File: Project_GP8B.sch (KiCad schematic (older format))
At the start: 11 parts, among them U1 74AHC05, U2 74AHC05, U3 74AHC1G04, U4 74AHC1G04, U5 74AHC05

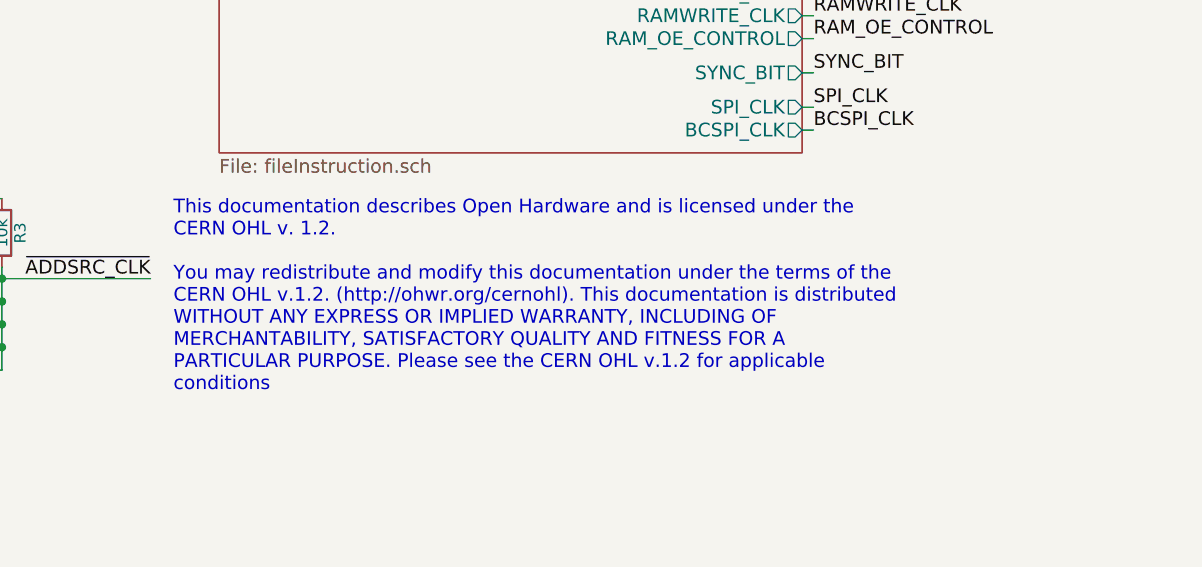
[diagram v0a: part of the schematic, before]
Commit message: Switching license to "CERN-OHLw v2 or later"
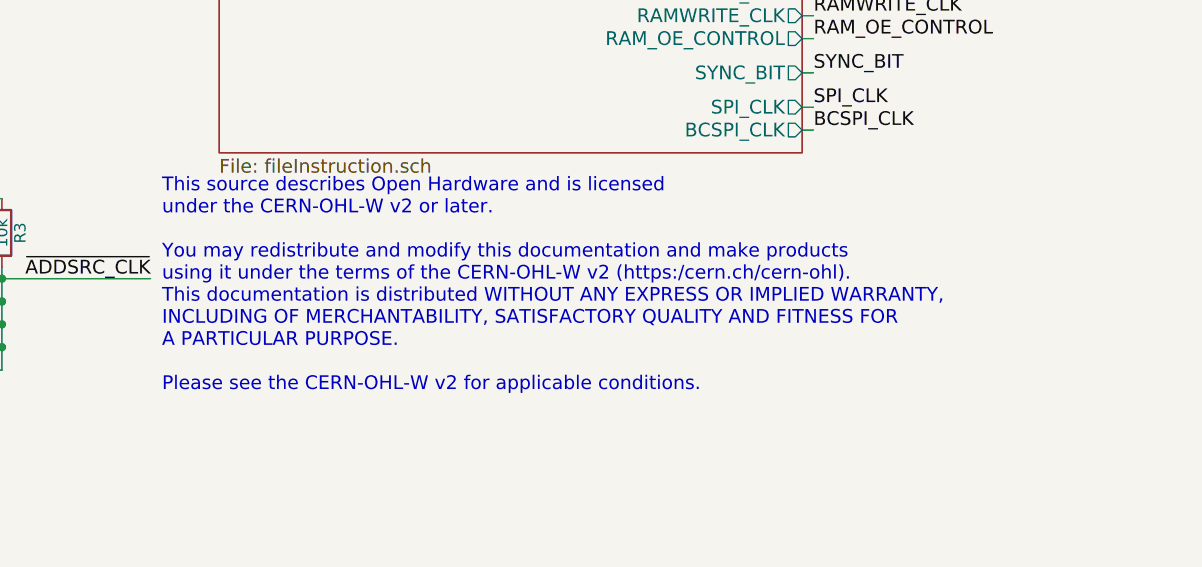
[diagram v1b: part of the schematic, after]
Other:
- note added: "This source describes Open Hardware and is licensed\nunder the CERN-OHL-W v2 or later. \n\nYou may redistribute and modify this documentation and make products\nusing it under the terms of the CERN-OHL-W v2 (https:/cern.ch/cern-ohl).\nThis documentation is distributed WITHOUT ANY EXPRESS OR IMPLIED WARRANTY,\nINCLUDING OF MERCHANTABILITY, SATISFACTORY QUALITY AND FITNESS FOR\nA PARTICULAR PURPOSE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"
- note removed: "This documentation describes Open Hardware and is licensed under the\nCERN OHL v. 1.2.\n\nYou may redistribute and modify this documentation under the terms of the\nCERN OHL v.1.2. (http://ohwr.org/cernohl). This documentation is distributed\nWITHOUT ANY EXPRESS OR IMPLIED WARRANTY, INCLUDING OF\nMERCHANTABILITY, SATISFACTORY QUALITY AND FITNESS FOR A\nPARTICULAR PURPOSE. Please see the CERN OHL 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"
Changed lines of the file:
@@
 Comp "Guillaume Guillet"
 Comment1 "Copyright Guillaume Guillet 2020"
-Comment2 "Licensed under CERN OHL v.1.2"
+Comment2 "Licensed under CERN-OHL-W v2 or later"
 Comment3 ""
 Comment4 ""
@@
 Text Label 10350 5300 0    60   ~ 0
 BCSPI_CLK
-Text Notes 7550 6450 0    60   ~ 0
-This documentation describes Open Hardware and is licensed under the\nCERN OHL v. 1.2.\n\nYou may redistribute and modify this documentation under the terms of the\nCERN OHL v.1.2. (http://ohwr.org/cernohl). This documentation is distributed\nWITHOUT ANY EXPRESS OR IMPLIED WARRANTY, INCLUDING OF\nMERCHANTABILITY, SATISFACTORY QUALITY AND FITNESS FOR A\nPARTICULAR PURPOSE. Please see the CERN OHL v.1.2 for applicable\nconditions
+Text Notes 7500 6450 0    60   ~ 0
+This source describes Open Hardware and is licensed\nunder the CERN-OHL-W v2 or later. \n\nYou may redistribute and modify this documentation and make products\nusing it under the terms of the CERN-OHL-W v2 (https:/cern.ch/cern-ohl).\nThis documentation is distributed WITHOUT ANY EXPRESS OR IMPLIED WARRANTY,\nINCLUDING OF MERCHANTABILITY, SATISFACTORY QUALITY AND FITNESS FOR\nA PARTICULAR PURPOSE.\n\nPlease see the CERN-OHL-W v2 for applicable conditions.
 Wire Bus Line
 	1700 2800 1700 3600

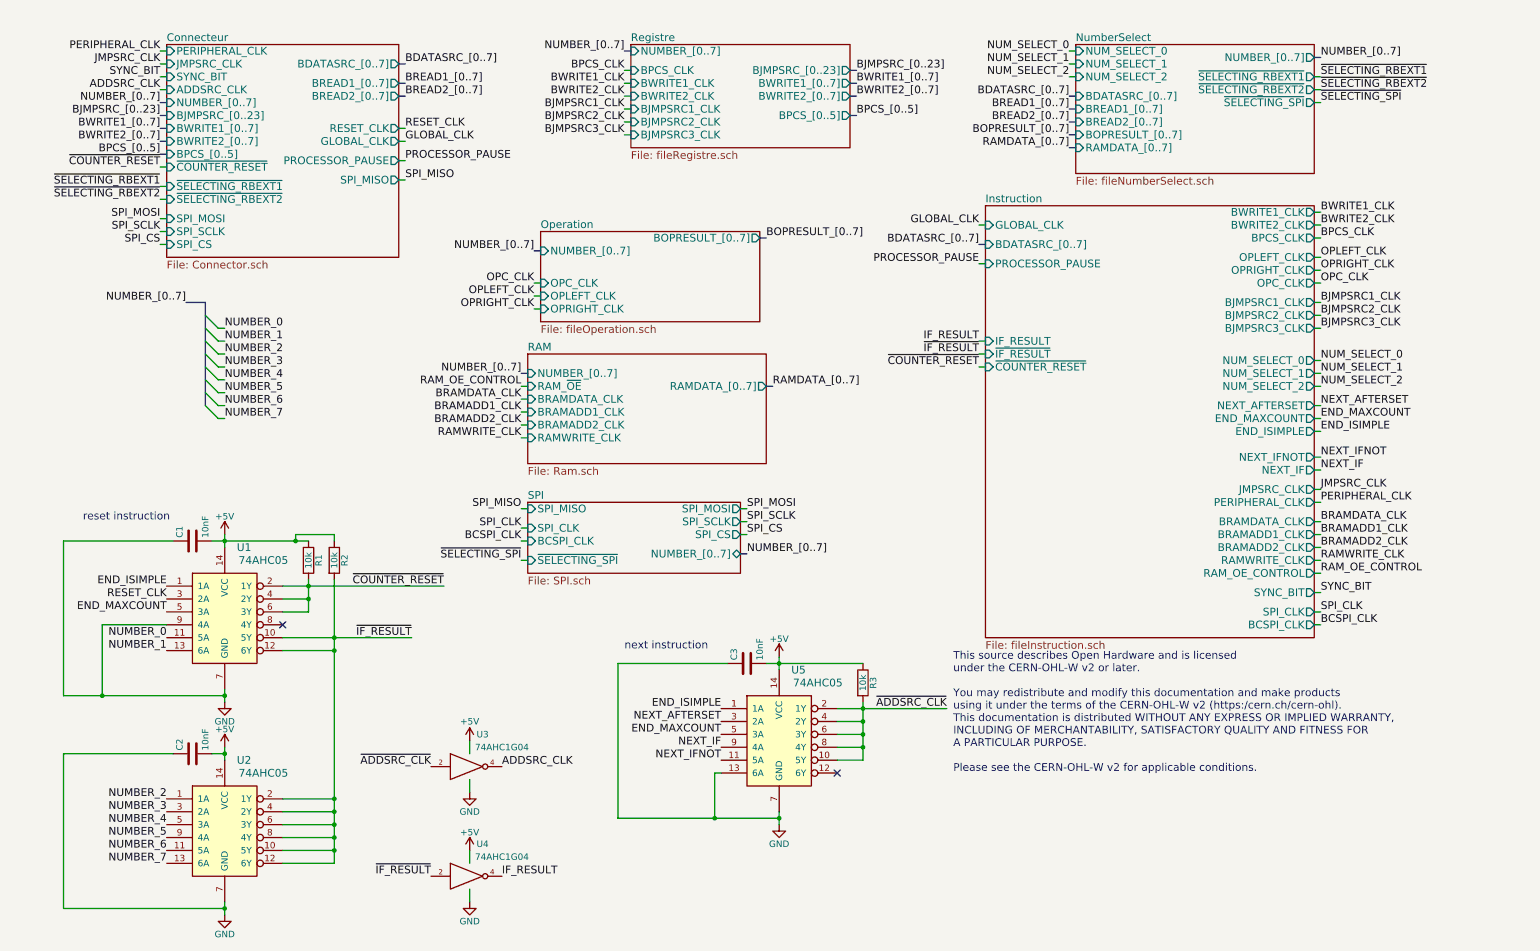
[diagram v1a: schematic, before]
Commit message: Small clean and mounting holes
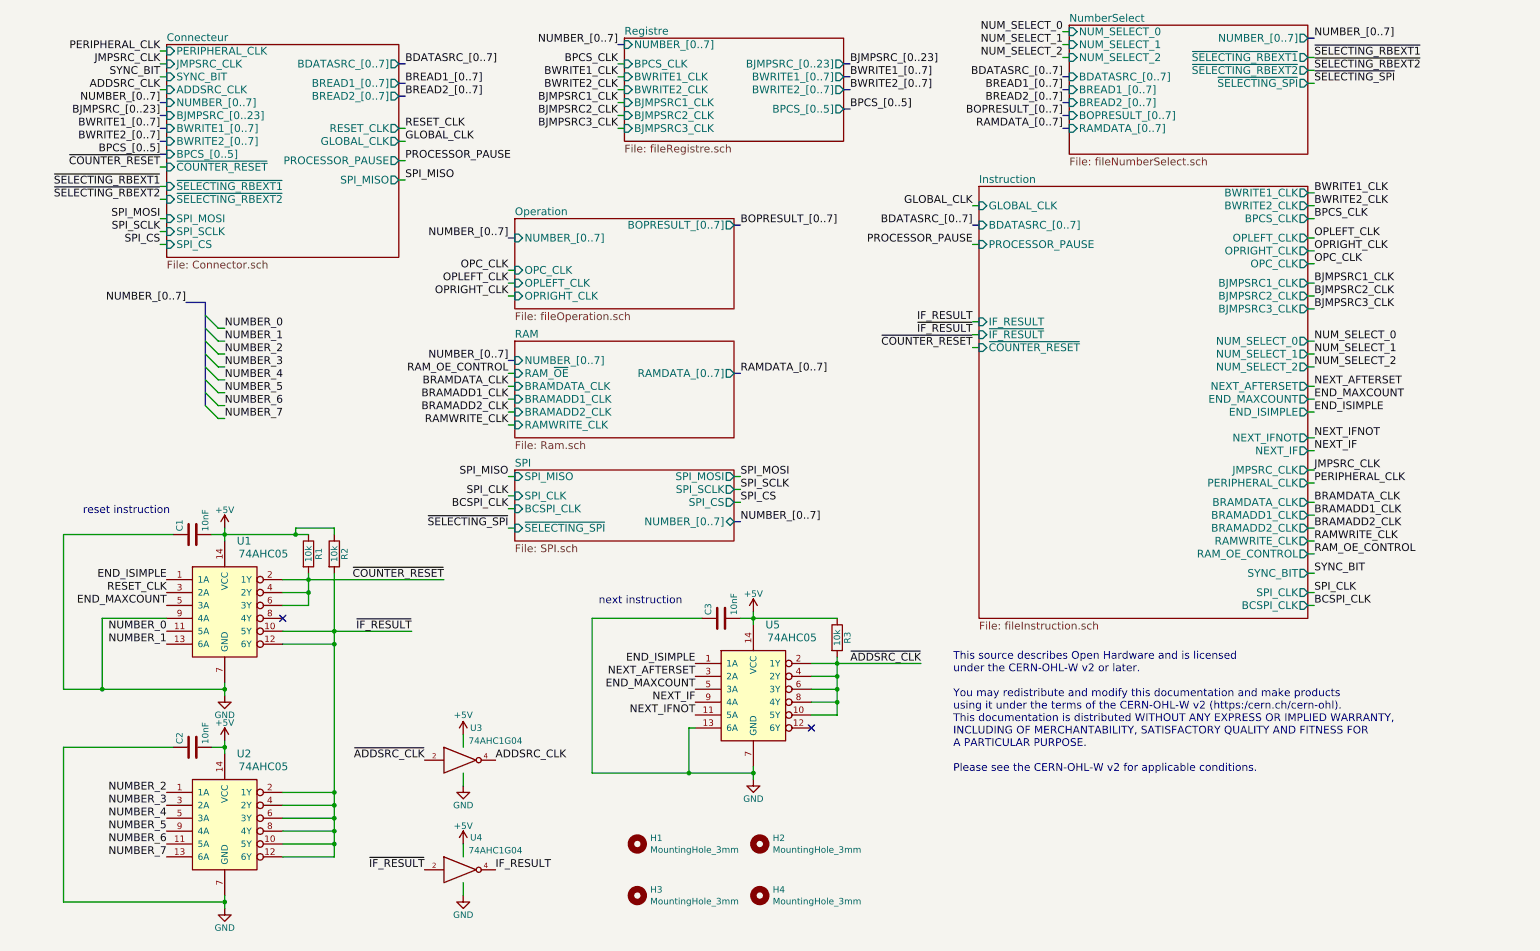
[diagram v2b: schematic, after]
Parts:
- added H1, H2, H3, H4: MountingHole_3mm, symbol Mechanical:MountingHole
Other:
- moved on the sheet: C1, C2, C3, R1, R2, R3, U1, U2, U3, U4, U5

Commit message: Renaming files, cleaning, CHANGELOG
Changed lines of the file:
@@
 F2 "BOPRESULT_[0..7]" O R 5800 2200 60
 F3 "NUMBER_[0..7]" I L 4100 2300 60
-F4 "OPC_CLK" I L 4100 2550 60
+F4 "OPCHOOSE_CLK" I L 4100 2550 60
 F5 "OPLEFT_CLK" I L 4100 2650 60
 F6 "OPRIGHT_CLK" I L 4100 2750 60
@@
 S 4950 750  1700 800
 U 5ACA3361
-F0 "Registre" 60
-F1 "fileRegistre.sch" 60
+F0 "Register" 60
+F1 "fileRegister.sch" 60
 F2 "NUMBER_[0..7]" I L 4950 800 60
 F3 "BWRITE1_[0..7]" O R 6650 1050 60
@@
 OPRIGHT_CLK
 Text Label 10300 2500 0    60   ~ 0
-OPC_CLK
+OPCHOOSE_CLK
 Text Label 10300 3850 0    60   ~ 0
 NEXT_IFNOT
@@
 Text Label 6700 950  0    60   ~ 0
 BJMPSRC_[0..23]
-$Sheet
-S 1400 800  1800 1650
-U 5B11F21F
-F0 "Connecteur" 60
-F1 "Connector.sch" 60
-F2 "RESET_CLK" O R 3200 1450 60
-F3 "SYNC_BIT" I L 1400 1050 60
-F4 "GLOBAL_CLK" O R 3200 1550 60
-F5 "NUMBER_[0..7]" I L 1400 1250 60
-F6 "BWRITE1_[0..7]" I L 1400 1450 60
-F7 "BWRITE2_[0..7]" I L 1400 1550 60
-F8 "BREAD1_[0..7]" O R 3200 1100 60
-F9 "BREAD2_[0..7]" O R 3200 1200 60
-F10 "~COUNTER_RESET" I L 1400 1750 60
-F11 "BPCS_[0..5]" I L 1400 1650 60
-F12 "BJMPSRC_[0..23]" I L 1400 1350 60
-F13 "BDATASRC_[0..7]" O R 3200 950 60
-F14 "PERIPHERAL_CLK" I L 1400 850 60
-F15 "JMPSRC_CLK" I L 1400 950 60
-F16 "ADDSRC_CLK" I L 1400 1150 60
-F17 "~SELECTING_RBEXT1" I L 1400 1900 60
-F18 "~SELECTING_RBEXT2" I L 1400 2000 60
-F19 "PROCESSOR_PAUSE" O R 3200 1700 60
-F20 "SPI_MISO" O R 3200 1850 60
-F21 "SPI_MOSI" I L 1400 2150 60
-F22 "SPI_SCLK" I L 1400 2250 60
-F23 "SPI_CS" I L 1400 2350 60
-$EndSheet
 Text Label 3250 1100 0    60   ~ 0
 BREAD1_[0..7]
@@
 U 5B0E1E98
 F0 "RAM" 60
-F1 "Ram.sch" 60
+F1 "fileRAM.sch" 60
 F2 "RAM_~OE" I L 4100 3350 60
 F3 "RAMDATA_[0..7]" O R 5800 3350 60
@@
 F22 "OPLEFT_CLK" O R 10250 2300 60
 F23 "OPRIGHT_CLK" O R 10250 2400 60
-F24 "OPC_CLK" O R 10250 2500 60
-F25 "BRAMDATA_CLK" O R 10250 4350 60
-F26 "RAMWRITE_CLK" O R 10250 4650 60
-F27 "BRAMADD2_CLK" O R 10250 4550 60
-F28 "BRAMADD1_CLK" O R 10250 4450 60
-F29 "NEXT_IF" O R 10250 3950 60
-F30 "NEXT_IFNOT" O R 10250 3850 60
-F31 "END_MAXCOUNT" O R 10250 3550 60
-F32 "NEXT_AFTERSET" O R 10250 3450 60
-F33 "END_ISIMPLE" O R 10250 3650 60
-F34 "BCSPI_CLK" O R 10250 5150 60
+F24 "BRAMDATA_CLK" O R 10250 4350 60
+F25 "RAMWRITE_CLK" O R 10250 4650 60
+F26 "BRAMADD2_CLK" O R 10250 4550 60
+F27 "BRAMADD1_CLK" O R 10250 4450 60
+F28 "NEXT_IF" O R 10250 3950 60
+F29 "NEXT_IFNOT" O R 10250 3850 60
+F30 "END_MAXCOUNT" O R 10250 3550 60
+F31 "NEXT_AFTERSET" O R 10250 3450 60
+F32 "END_ISIMPLE" O R 10250 3650 60
+F33 "OPCHOOSE_CLK" O R 10250 2500 60
+F34 "BCFG_SPI_CLK" O R 10250 5150 60
 $EndSheet
 Text Label 7250 5600 2    60   ~ 0
@@
 U 5DD53CC6
 F0 "SPI" 60
-F1 "SPI.sch" 60
+F1 "fileSPI.sch" 60
 F2 "SPI_MISO" I L 4100 4150 60
 F3 "SPI_MOSI" O R 5800 4150 60
@@
 F7 "NUMBER_[0..7]" B R 5800 4500 60
 F8 "~SELECTING_SPI" I L 4100 4550 60
-F9 "BCSPI_CLK" I L 4100 4400 60
+F9 "BCFG_SPI_CLK" I L 4100 4400 60
 $EndSheet
 Text Label 5850 4350 0    60   ~ 0
@@
 Text Label 4050 4300 2    60   ~ 0
 SPI_CLK
-Text Label 4050 4400 2    60   ~ 0
-BCSPI_CLK
 Text Label 4050 4550 2    60   ~ 0
 ~SELECTING_SPI
@@
 Text Label 4050 2750 2    60   ~ 0
 OPRIGHT_CLK
-Text Label 4050 2550 2    60   ~ 0
-OPC_CLK
 Text Label 4050 3450 2    60   ~ 0
 BRAMDATA_CLK
@@
 	5450 6450 5950 6450
 Text Label 10300 5150 0    60   ~ 0
-BCSPI_CLK
+BCFG_SPI_CLK
 Text Notes 7500 6450 0    60   ~ 0
 This source describes Open Hardware and is licensed\nunder the CERN-OHL-W v2 or later. \n\nYou may redistribute and modify this documentation and make products\nusing it under the terms of the CERN-OHL-W v2 (https:/cern.ch/cern-ohl).\nThis documentation is distributed WITHOUT ANY EXPRESS OR IMPLIED WARRANTY,\nINCLUDING OF MERCHANTABILITY, SATISFACTORY QUALITY AND FITNESS FOR\nA PARTICULAR PURPOSE.\n\nPlease see the CERN-OHL-W v2 for applicable conditions.
@@
 	1    0    0    -1
 $EndComp
+Text Label 4050 2550 2    60   ~ 0
+OPCHOOSE_CLK
+Text Label 4050 4400 2    60   ~ 0
+BCFG_SPI_CLK
 Wire Bus Line
 	1700 2800 1700 3600
+$Sheet
+S 1400 800  1800 1650
+U 5B11F21F
+F0 "Connector" 60
+F1 "fileConnector.sch" 60
+F2 "RESET_CLK" O R 3200 1450 60
+F3 "SYNC_BIT" I L 1400 1050 60
+F4 "GLOBAL_CLK" O R 3200 1550 60
+F5 "NUMBER_[0..7]" I L 1400 1250 60
+F6 "BWRITE1_[0..7]" I L 1400 1450 60
+F7 "BWRITE2_[0..7]" I L 1400 1550 60
+F8 "BREAD1_[0..7]" O R 3200 1100 60
+F9 "BREAD2_[0..7]" O R 3200 1200 60
+F10 "~COUNTER_RESET" I L 1400 1750 60
+F11 "BPCS_[0..5]" I L 1400 1650 60
+F12 "BJMPSRC_[0..23]" I L 1400 1350 60
+F13 "BDATASRC_[0..7]" O R 3200 950 60
+F14 "PERIPHERAL_CLK" I L 1400 850 60
+F15 "JMPSRC_CLK" I L 1400 950 60
+F16 "ADDSRC_CLK" I L 1400 1150 60
+F17 "~SELECTING_RBEXT1" I L 1400 1900 60
+F18 "~SELECTING_RBEXT2" I L 1400 2000 60
+F19 "PROCESSOR_PAUSE" O R 3200 1700 60
+F20 "SPI_MISO" O R 3200 1850 60
+F21 "SPI_MOSI" I L 1400 2150 60
+F22 "SPI_SCLK" I L 1400 2250 60
+F23 "SPI_CS" I L 1400 2350 60
+$EndSheet
 $EndSCHEMATC

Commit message: Cleaning
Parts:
- H1, H2, H3, H4: footprint (none) -> MountingHole:MountingHole_3mm
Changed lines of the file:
@@
 F 0 "H1" H 5150 7046 50  0000 L CNN
 F 1 "MountingHole_3mm" H 5150 6955 50  0000 L CNN
-F 2 "" H 5050 7000 50  0001 C CNN
+F 2 "MountingHole:MountingHole_3mm" H 5050 7000 50  0001 C CNN
 F 3 "~" H 5050 7000 50  0001 C CNN
 	1    5050 7000
@@
 F 0 "H3" H 5150 7446 50  0000 L CNN
 F 1 "MountingHole_3mm" H 5150 7355 50  0000 L CNN
-F 2 "" H 5050 7400 50  0001 C CNN
+F 2 "MountingHole:MountingHole_3mm" H 5050 7400 50  0001 C CNN
 F 3 "~" H 5050 7400 50  0001 C CNN
 	1    5050 7400
@@
 F 0 "H4" H 6100 7446 50  0000 L CNN
 F 1 "MountingHole_3mm" H 6100 7355 50  0000 L CNN
-F 2 "" H 6000 7400 50  0001 C CNN
+F 2 "MountingHole:MountingHole_3mm" H 6000 7400 50  0001 C CNN
 F 3 "~" H 6000 7400 50  0001 C CNN
 	1    6000 7400
@@
 F 0 "H2" H 6100 7046 50  0000 L CNN
 F 1 "MountingHole_3mm" H 6100 6955 50  0000 L CNN
-F 2 "" H 6000 7000 50  0001 C CNN
+F 2 "MountingHole:MountingHole_3mm" H 6000 7000 50  0001 C CNN
 F 3 "~" H 6000 7000 50  0001 C CNN
 	1    6000 7000
@@
 Text Label 4050 4400 2    60   ~ 0
 BCFG_SPI_CLK
-Wire Bus Line
-	1700 2800 1700 3600
 $Sheet
 S 1400 800  1800 1650
@@
 F23 "SPI_CS" I L 1400 2350 60
 $EndSheet
+Wire Bus Line
+	1700 2800 1700 3600
 $EndSCHEMATC
